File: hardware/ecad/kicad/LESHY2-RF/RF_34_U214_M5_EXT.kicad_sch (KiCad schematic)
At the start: 0 parts

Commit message: complete exact H2.3.1 RF power hierarchy
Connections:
- no-connect marks 0 -> 26

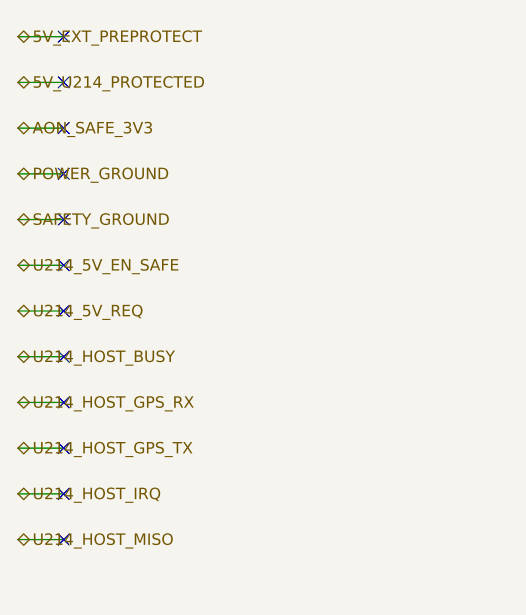
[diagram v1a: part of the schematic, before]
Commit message: complete exact H2.3.4 power rails
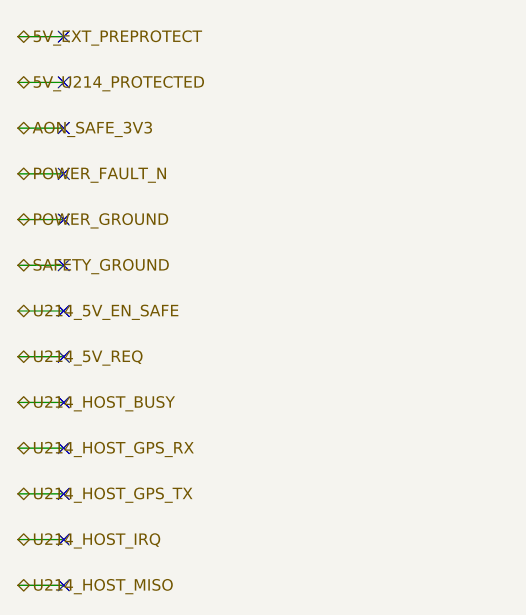
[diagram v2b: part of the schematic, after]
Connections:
- no-connect marks 26 -> 27
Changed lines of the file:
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@@
 	(no_connect (at 25.40 35.56)
 	)
-	(hierarchical_label "POWER_GROUND"
+	(hierarchical_label "POWER_FAULT_N"
 		(shape bidirectional)
 		(at 20.32 40.64 0)
@@
 	(no_connect (at 25.40 40.64)
 	)
-	(hierarchical_label "SAFETY_GROUND"
+	(hierarchical_label "POWER_GROUND"
 		(shape bidirectional)
 		(at 20.32 45.72 0)
@@
 	(no_connect (at 25.40 45.72)
 	)
-	(hierarchical_label "U214_5V_EN_SAFE"
+	(hierarchical_label "SAFETY_GROUND"
 		(shape bidirectional)
 		(at 20.32 50.80 0)
@@
 	(no_connect (at 25.40 50.80)
 	)
-	(hierarchical_label "U214_5V_REQ"
+	(hierarchical_label "U214_5V_EN_SAFE"
 		(shape bidirectional)
 		(at 20.32 55.88 0)
@@
 	(no_connect (at 25.40 55.88)
 	)
-	(hierarchical_label "U214_HOST_BUSY"
+	(hierarchical_label "U214_5V_REQ"
 		(shape bidirectional)
 		(at 20.32 60.96 0)
@@
 	(no_connect (at 25.40 60.96)
 	)
-	(hierarchical_label "U214_HOST_GPS_RX"
+	(hierarchical_label "U214_HOST_BUSY"
 		(shape bidirectional)
 		(at 20.32 66.04 0)
@@
 	(no_connect (at 25.40 66.04)
 	)
-	(hierarchical_label "U214_HOST_GPS_TX"
+	(hierarchical_label "U214_HOST_GPS_RX"
 		(shape bidirectional)
 		(at 20.32 71.12 0)
@@
 	(no_connect (at 25.40 71.12)
 	)
-	(hierarchical_label "U214_HOST_IRQ"
+	(hierarchical_label "U214_HOST_GPS_TX"
 		(shape bidirectional)
 		(at 20.32 76.20 0)
@@
 	(no_connect (at 25.40 76.20)
 	)
-	(hierarchical_label "U214_HOST_MISO"
+	(hierarchical_label "U214_HOST_IRQ"
 		(shape bidirectional)
 		(at 20.32 81.28 0)
@@
 	(no_connect (at 25.40 81.28)
 	)
+	(hierarchical_label "U214_HOST_MISO"
+		(shape bidirectional)
+		(at 20.32 86.36 0)
+		(effects (font (size 1.27 1.27)))
+	)
+	(wire
+		(pts (xy 20.32 86.36) (xy 25.40 86.36))
+		(stroke (width 0) (type default))
+	)
+	(no_connect (at 25.40 86.36)
+	)
 	(hierarchical_label "U214_HOST_MOSI"

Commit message: complete exact H2.3.8 U214 and M5 expansion sheet
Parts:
- added C1: TDK C1005X7R1H104K050BB, Capacitor_SMD:C_0402_1005Metric, symbol Leshy2:RF34_U214_I2C_ISO_BYPASS
- added C10: Murata GRM21BR71E225KE11L, Capacitor_SMD:C_0805_2012Metric, symbol Leshy2:RF34_UNIT_OUTPUT_CAP
- added C11: TDK C1005X7R1H104K050BB, Capacitor_SMD:C_0402_1005Metric, symbol Leshy2:RF34_UNIT_SUPERVISOR_BYPASS
- added C12: Murata GRM155R71H103KA88D, Capacitor_SMD:C_0402_1005Metric, symbol Leshy2:RF34_UNIT_SUPERVISOR_CT
- added C13: TDK C1005X7R1H104K050BB, Capacitor_SMD:C_0402_1005Metric, symbol Leshy2:RF34_UNIT_SIGNAL_ISO_VCCA_BYPASS
- added C14: TDK C1005X7R1H104K050BB, Capacitor_SMD:C_0402_1005Metric, symbol Leshy2:RF34_UNIT_SIGNAL_ISO_VCCB_BYPASS
- added C2: TDK C1005X7R1H104K050BB, Capacitor_SMD:C_0402_1005Metric, symbol Leshy2:RF34_U214_HOST_BUFFER_A_BYPASS
- added C3: TDK C1005X7R1H104K050BB, Capacitor_SMD:C_0402_1005Metric, symbol Leshy2:RF34_U214_HOST_BUFFER_B_BYPASS
- added C4: TDK C1005X7R1H104K050BB, Capacitor_SMD:C_0402_1005Metric, symbol Leshy2:RF34_U214_RETURN_BUFFER_BYPASS
- added C5: TDK C1005X7R1H104K050BB, Capacitor_SMD:C_0402_1005Metric, symbol Leshy2:RF34_U214_SUPERVISOR_BYPASS
- added C6: Murata GRM155R71H103KA88D, Capacitor_SMD:C_0402_1005Metric, symbol Leshy2:RF34_U214_SUPERVISOR_CT
- added C7: Murata GRM155R71H472KA01D, Capacitor_SMD:C_0402_1005Metric, symbol Leshy2:RF34_UNIT_DVDT_CAP
- added C8: Murata GRM188R71E224KA88D, Capacitor_SMD:C_0603_1608Metric, symbol Leshy2:RF34_UNIT_ITIMER_CAP
- added C9: Murata GRM21BR71E225KE11L, Capacitor_SMD:C_0805_2012Metric, symbol Leshy2:RF34_UNIT_INPUT_CAP
- added J1: Samtec HLE-107-02-G-DV-PE-LC, Connector_Samtec_HLE_THT:Samtec_HLE-107-02-xx-DV-PE-LC_2x07_P2.54mm_Horizontal, symbol Leshy2:RF34_U214_CONNECTOR
- added J2: 1125R-SMT-4P, Leshy2:1125R-SMT-4P, symbol Leshy2:RF34_UNIT_CONNECTOR
- added R1: Yageo RC0402FR-072K2L, Resistor_SMD:R_0402_1005Metric, symbol Leshy2:RF34_U214_I2C_HOST_SDA_PULLUP
- added R10: Panasonic ERJ-2RKF22R0X, Resistor_SMD:R_0402_1005Metric, symbol Leshy2:RF34_U214_SERIES_GPS_TX
- added R11: Panasonic ERJ-2RKF22R0X, Resistor_SMD:R_0402_1005Metric, symbol Leshy2:RF34_U214_SERIES_MISO
- added R12: Yageo RC0402FR-0710KL, Resistor_SMD:R_0402_1005Metric, symbol Leshy2:RF34_U214_REQ_PULLDOWN
- added R13: Yageo RC0402FR-0710KL, Resistor_SMD:R_0402_1005Metric, symbol Leshy2:RF34_UNIT_REQ_PULLDOWN
- added R14: Yageo RC0402FR-07110KL, Resistor_SMD:R_0402_1005Metric, symbol Leshy2:RF34_U214_SUPERVISOR_SENSE_TOP
- added R15: Yageo RC0402FR-07220KL, Resistor_SMD:R_0402_1005Metric, symbol Leshy2:RF34_U214_SUPERVISOR_SENSE_BOTTOM
- added R16: Yageo RC0402FR-0710KL, Resistor_SMD:R_0402_1005Metric, symbol Leshy2:RF34_U214_SUPERVISOR_PULLUP
- added R17: Yageo RC0402FR-072K21L, Resistor_SMD:R_0402_1005Metric, symbol Leshy2:RF34_UNIT_RILM
- added R18: Yageo RC0402FR-07169KL, Resistor_SMD:R_0402_1005Metric, symbol Leshy2:RF34_UNIT_OVLO_TOP
- added R19: Yageo RC0402FR-0747KL, Resistor_SMD:R_0402_1005Metric, symbol Leshy2:RF34_UNIT_OVLO_BOTTOM
- added R2: Yageo RC0402FR-072K2L, Resistor_SMD:R_0402_1005Metric, symbol Leshy2:RF34_U214_I2C_HOST_SCL_PULLUP
- added R20: Yageo RC0603FR-071KL, Resistor_SMD:R_0603_1608Metric, symbol Leshy2:RF34_UNIT_BLEEDER
- added R21: Yageo RC0402FR-07110KL, Resistor_SMD:R_0402_1005Metric, symbol Leshy2:RF34_UNIT_SUPERVISOR_SENSE_TOP
- added R22: Yageo RC0402FR-07220KL, Resistor_SMD:R_0402_1005Metric, symbol Leshy2:RF34_UNIT_SUPERVISOR_SENSE_BOTTOM
- added R23: Yageo RC0402FR-0710KL, Resistor_SMD:R_0402_1005Metric, symbol Leshy2:RF34_UNIT_SUPERVISOR_PULLUP
- added R24: Yageo RC0402FR-0710KL, Resistor_SMD:R_0402_1005Metric, symbol Leshy2:RF34_UNIT_SIGNAL_ISO_OE_PULLDOWN
- added R3: Panasonic ERJ-2RKF22R0X, Resistor_SMD:R_0402_1005Metric, symbol Leshy2:RF34_U214_SERIES_RST
- added R4: Panasonic ERJ-2RKF22R0X, Resistor_SMD:R_0402_1005Metric, symbol Leshy2:RF34_U214_SERIES_GPS_RX
- added R5: Panasonic ERJ-2RKF22R0X, Resistor_SMD:R_0402_1005Metric, symbol Leshy2:RF34_U214_SERIES_SCK
- added R6: Panasonic ERJ-2RKF22R0X, Resistor_SMD:R_0402_1005Metric, symbol Leshy2:RF34_U214_SERIES_MOSI
- added R7: Panasonic ERJ-2RKF22R0X, Resistor_SMD:R_0402_1005Metric, symbol Leshy2:RF34_U214_SERIES_NSS
- added R8: Panasonic ERJ-2RKF22R0X, Resistor_SMD:R_0402_1005Metric, symbol Leshy2:RF34_U214_SERIES_BUSY
- added R9: Panasonic ERJ-2RKF22R0X, Resistor_SMD:R_0402_1005Metric, symbol Leshy2:RF34_U214_SERIES_IRQ
- added U1: TCA4307DGKR, Package_SO:VSSOP-8_3x3mm_P0.65mm, symbol Leshy2:RF34_U214_I2C_ISO
- added U10: TPS3808G33DBVR, Package_TO_SOT_SMD:SOT-23-6, symbol Leshy2:RF34_UNIT_SUPERVISOR
- added U11: Texas Instruments TXS0102DCUR, Package_SO:VSSOP-8_2.3x2mm_P0.5mm, symbol Leshy2:RF34_UNIT_SIGNAL_ISO
- added U12: Texas Instruments TPD4E05U06DQAR, Package_SON:USON-10_2.5x1.0mm_P0.5mm, symbol Leshy2:RF34_UNIT_ESD
- added U2: Nexperia 74LVC126APW,118, Package_SO:TSSOP-14_4.4x5mm_P0.65mm, symbol Leshy2:RF34_U214_HOST_BUFFER_A
- added U3: Nexperia 74LVC126APW,118, Package_SO:TSSOP-14_4.4x5mm_P0.65mm, symbol Leshy2:RF34_U214_HOST_BUFFER_B
- added U4: Nexperia 74LVC126APW,118, Package_SO:TSSOP-14_4.4x5mm_P0.65mm, symbol Leshy2:RF34_U214_RETURN_BUFFER
- added U5: Texas Instruments TPD4E05U06DQAR, Package_SON:USON-10_2.5x1.0mm_P0.5mm, symbol Leshy2:RF34_U214_ESD_A
- added U6: Texas Instruments TPD4E05U06DQAR, Package_SON:USON-10_2.5x1.0mm_P0.5mm, symbol Leshy2:RF34_U214_ESD_B
- added U7: Texas Instruments TPD4E05U06DQAR, Package_SON:USON-10_2.5x1.0mm_P0.5mm, symbol Leshy2:RF34_U214_ESD_C
- added U8: TPS3808G33DBVR, Package_TO_SOT_SMD:SOT-23-6, symbol Leshy2:RF34_U214_SUPERVISOR
- added U9: Texas Instruments TPS259470LRPWR, Leshy2:TI-RPW0010A-VQFN-HR-10, symbol Leshy2:RF34_UNIT_EFUSE
- added X1: M5Stack U214 Cap LoRa-1262, symbol Leshy2:RF34_U214
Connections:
- net 3V3_MAIN: now also C1.1 (END_1), C13.1 (END_1), C14.1 (END_1), C2.1 (END_1), C3.1 (END_1), C4.1 (END_1), R1.1 (END_1), R16.1 (END_1), R2.1 (END_1), R23.1 (END_1), U1.8 (VCC), U11.1 (VCCA), U11.7 (VCCB), U2.14 (VCC), U3.14 (VCC), U4.14 (VCC)
- net 5V_EXT_PREPROTECT: now also C9.1 (END_1), R18.1 (END_1), U9.5 (IN)
- net 5V_U214_PROTECTED: now also J1.7 (PIN_7), R14.1 (END_1), X1.7 (5V_IN)
- net AON_SAFE_3V3: now also C11.1 (END_1), C5.1 (END_1), U10.6 (VDD), U8.6 (VDD)
- net POWER_FAULT_N: now also U9.4 (FLT)
- net POWER_GROUND: now also C1.2 (END_2), C10.2 (END_2), C13.2 (END_2), C14.2 (END_2), C2.2 (END_2), C3.2 (END_2), C4.2 (END_2), C7.2 (END_2), C8.2 (END_2), C9.2 (END_2), J1.6 (PIN_6), J2.1 (GND), R12.2 (END_2), R13.2 (END_2), R17.2 (END_2), R19.2 (END_2), R20.2 (END_2), R24.2 (END_2), U1.4 (GND), U11.4 (GND), U12.3 (GND_3), U12.8 (GND_8), U2.7 (GND), U3.10 (3OE), U3.12 (4A), U3.13 (4OE), U3.4 (2OE), U3.5 (2A), U3.7 (GND), U3.9 (3A), U4.7 (GND), U5.3 (GND_3), U5.8 (GND_8), U6.3 (GND_3), U6.8 (GND_8), U7.3 (GND_3), U7.8 (GND_8), U9.8 (GND), X1.6 (GND)
- net SAFETY_GROUND: now also C11.2 (END_2), C12.2 (END_2), C5.2 (END_2), C6.2 (END_2), R15.2 (END_2), R22.2 (END_2), U10.2 (GND), U8.2 (GND)
- net U214_5V_EN_SAFE: now also U8.3 (MR_N)
- net U214_5V_REQ: now also R12.1 (END_1)
- net U214_HOST_BUSY: now also R8.2 (END_2)
- net U214_HOST_GPS_RX: now also R10.2 (END_2)
- net U214_HOST_GPS_TX: now also U2.5 (2A)
- net U214_HOST_IRQ: now also R9.2 (END_2)
- net U214_HOST_MISO: now also R11.2 (END_2)
- net U214_HOST_MOSI: now also U2.12 (4A)
- net U214_HOST_NSS_N: now also U3.2 (1A)
- net U214_HOST_RST_N: now also U2.2 (1A)
- net U214_HOST_SCK: now also U2.9 (3A)
- net U214_I2C_READY: now also U1.5 (READY)
- net U214_I2C_SCL_IN: now also R2.2 (END_2), U1.3 (SCLIN)
- net U214_I2C_SDA_IN: now also R1.2 (END_2), U1.6 (SDAIN)
- net U214_PIN5_PROFILE: now also J1.5 (PIN_5), U7.5 (D2_MINUS), X1.5 (5V_OUT)
- net UNIT_5V_EN_SAFE: now also U10.3 (MR_N), U9.1 (EN_UVLO)
- net UNIT_5V_REQ: now also R13.1 (END_1)
- net UNIT_HOST_SIG0: now also U11.2 (A1)
- net UNIT_HOST_SIG1: now also U11.3 (A2)
- net UNIT_READY: now also R23.2 (END_2), R24.1 (END_1), U10.1 (RESET_N), U11.8 (OE)
- new net 5V_UNIT_PROTECTED: C10.1 (END_1), J2.2 (5V), R20.1 (END_1), R21.1 (END_1), U9.6 (OUT)
- new net U214_5V_SENSE: R14.2 (END_2), R15.1 (END_1), U8.5 (SENSE)
- new net U214_BUSY_BUFFERED: R8.1 (END_1), U4.3 (1Y)
- new net U214_BUSY_CONNECTOR: J1.10 (PIN_10), U4.2 (1A), U6.5 (D2_MINUS), X1.10 (LORA_BUSY)
- new net U214_GPS_RX_BUFFERED: R4.1 (END_1), U2.6 (2Y)
- new net U214_GPS_RX_CONNECTOR: J1.2 (PIN_2), R4.2 (END_2), U5.5 (D2_MINUS), X1.2 (GPS_RX)
- new net U214_GPS_TX_BUFFERED: R10.1 (END_1), U4.8 (3Y)
- new net U214_GPS_TX_CONNECTOR: J1.1 (PIN_1), U4.9 (3A), U7.2 (D1_MINUS), X1.1 (GPS_TX)
- new net U214_I2C_SCL_OUT: J1.3 (PIN_3), U1.2 (SCLOUT), U5.2 (D1_MINUS), X1.3 (SCL)
- new net U214_I2C_SDA_OUT: J1.4 (PIN_4), U1.7 (SDAOUT), U5.1 (D1_PLUS), X1.4 (SDA)
- new net U214_IRQ_BUFFERED: R9.1 (END_1), U4.6 (2Y)
- new net U214_IRQ_CONNECTOR: J1.9 (PIN_9), U4.5 (2A), U7.1 (D1_PLUS), X1.9 (LORA_IRQ)
- new net U214_MISO_BUFFERED: R11.1 (END_1), U4.11 (4Y)
- new net U214_MISO_CONNECTOR: J1.13 (PIN_13), U4.12 (4A), U7.4 (D2_PLUS), X1.13 (MISO)
- new net U214_MOSI_BUFFERED: R6.1 (END_1), U2.11 (4Y)
- new net U214_MOSI_CONNECTOR: J1.12 (PIN_12), R6.2 (END_2), U6.2 (D1_MINUS), X1.12 (MOSI)
- new net U214_NSS_BUFFERED: R7.1 (END_1), U3.3 (1Y)
- new net U214_NSS_CONNECTOR: J1.14 (PIN_14), R7.2 (END_2), U6.4 (D2_PLUS), X1.14 (NSS)
- new net U214_READY: R16.2 (END_2), U1.1 (EN), U2.1 (1OE), U2.10 (3OE), U2.13 (4OE), U2.4 (2OE), U3.1 (1OE), U4.1 (1OE), U4.10 (3OE), U4.13 (4OE), U4.4 (2OE), U8.1 (RESET_N)
- new net U214_READY_DELAY: C6.1 (END_1), U8.4 (CT)
- new net U214_RST_BUFFERED: R3.1 (END_1), U2.3 (1Y)
- new net U214_RST_CONNECTOR: J1.8 (PIN_8), R3.2 (END_2), U5.4 (D2_PLUS), X1.8 (LORA_RST)
- new net U214_SCK_BUFFERED: R5.1 (END_1), U2.8 (3Y)
- new net U214_SCK_CONNECTOR: J1.11 (PIN_11), R5.2 (END_2), U6.1 (D1_PLUS), X1.11 (SCK)
- new net UNIT_5V_CURRENT_MONITOR: R17.1 (END_1), U9.9 (ILM)
- new net UNIT_5V_SENSE: R21.2 (END_2), R22.1 (END_1), U10.5 (SENSE)
- new net UNIT_CONNECTOR_SIG0: J2.3 (SIG0), U11.6 (B1), U12.1 (D1_PLUS)
- new net UNIT_CONNECTOR_SIG1: J2.4 (SIG1), U11.5 (B2), U12.2 (D1_MINUS)
- new net UNIT_EFUSE_DVDT: C7.1 (END_1), U9.7 (DVDT)
- new net UNIT_EFUSE_ITIMER: C8.1 (END_1), U9.10 (ITIMER)
- new net UNIT_EFUSE_OVLO_SENSE: R18.2 (END_2), R19.1 (END_1), U9.2 (OVLO)
- new net UNIT_READY_DELAY: C12.1 (END_1), U10.4 (CT)
- no-connect marks 27 -> 22
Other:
- title: (none) -> Leshy2 — isolated U214 Cap-Bus and native M5 Unit expansion

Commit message: complete H2 schematic review package
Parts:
- renumbered C1 to C34001, C2 to C34002, C3 to C34003, C4 to C34004, C5 to C34005, C6 to C34006, C7 to C34007, C8 to C34008, C9 to C34009, C10 to C34010, C11 to C34011, C12 to C34012, C13 to C34013, C14 to C34014, J1 to J34001, J2 to J34002, R1 to R34001, R2 to R34002, R3 to R34003, R4 to R34004, R5 to R34005, R6 to R34006, R7 to R34007, R8 to R34008, R9 to R34009, R10 to R34010, R11 to R34011, R12 to R34012, R13 to R34013, R14 to R34014, R15 to R34015, R16 to R34016, R17 to R34017, R18 to R34018, R19 to R34019, R20 to R34020, R21 to R34021, R22 to R34022, R23 to R34023, R24 to R34024, U1 to U34001, U2 to U34002, U3 to U34003, U4 to U34004, U5 to U34005, U6 to U34006, U7 to U34007, U8 to U34008, U9 to U34009, U10 to U34010, U11 to U34011, U12 to U34012, X1 to X34001

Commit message: docs: complete H3.1 steady power verification
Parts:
- R34017: value Yageo RC0402FR-072K21L -> Yageo RC0402FR-071K82L
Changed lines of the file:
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@@
 			(effects (font (size 1.27 1.27)))
 		)
-		(property "Value" "Yageo RC0402FR-072K21L"
+		(property "Value" "Yageo RC0402FR-071K82L"
 			(at 320.04 135.89 0)
 			(show_name no)
@@
 			(effects (font (size 1.27 1.27)))
 		)
-		(property "Description" "2_21kohm_1pct_0402_efuse_current_limit_resistor"
+		(property "Description" "1_82kohm_1pct_0402_efuse_current_limit_resistor"
 			(at 320.04 130.81 0)
 			(show_name no)

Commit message: Optimize H1 display and stocked BOM routes
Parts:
- C34001, C34002, C34003, C34004, C34005, C34011, C34013, C34014: value TDK C1005X7R1H104K050BB -> Yageo CC0402KRX7R9BB104
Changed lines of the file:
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@@
 			(effects (font (size 1.27 1.27)))
 		)
-		(property "Value" "TDK C1005X7R1H104K050BB"
+		(property "Value" "Yageo CC0402KRX7R9BB104"
 			(at 208.28 44.45 0)
 			(show_name no)
@@
 			(effects (font (size 1.27 1.27)))
 		)
-		(property "Value" "TDK C1005X7R1H104K050BB"
+		(property "Value" "Yageo CC0402KRX7R9BB104"
 			(at 264.16 67.31 0)
 			(show_name no)
@@
 			(effects (font (size 1.27 1.27)))
 		)
-		(property "Value" "TDK C1005X7R1H104K050BB"
+		(property "Value" "Yageo CC0402KRX7R9BB104"
 			(at 320.04 67.31 0)
 			(show_name no)
@@
 			(effects (font (size 1.27 1.27)))
 		)
-		(property "Value" "TDK C1005X7R1H104K050BB"
+		(property "Value" "Yageo CC0402KRX7R9BB104"
 			(at 152.40 72.39 0)
 			(show_name no)
@@
 			(effects (font (size 1.27 1.27)))
 		)
-		(property "Value" "TDK C1005X7R1H104K050BB"
+		(property "Value" "Yageo CC0402KRX7R9BB104"
 			(at 40.64 125.73 0)
 			(show_name no)
@@
 			(effects (font (size 1.27 1.27)))
 		)
-		(property "Value" "TDK C1005X7R1H104K050BB"
+		(property "Value" "Yageo CC0402KRX7R9BB104"
 			(at 152.40 166.37 0)
 			(show_name no)
@@
 			(effects (font (size 1.27 1.27)))
 		)
-		(property "Value" "TDK C1005X7R1H104K050BB"
+		(property "Value" "Yageo CC0402KRX7R9BB104"
 			(at 320.04 181.61 0)
 			(show_name no)
@@
 			(effects (font (size 1.27 1.27)))
 		)
-		(property "Value" "TDK C1005X7R1H104K050BB"
+		(property "Value" "Yageo CC0402KRX7R9BB104"
 			(at 152.40 189.23 0)
 			(show_name no)

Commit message: Replace six pre-order resistor identities
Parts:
- R34001, R34002: value Yageo RC0402FR-072K2L -> UNI-ROYAL 0402WGF2201TCE
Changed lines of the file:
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@@
 			(effects (font (size 1.27 1.27)))
 		)
-		(property "Value" "Yageo RC0402FR-072K2L"
+		(property "Value" "UNI-ROYAL 0402WGF2201TCE"
 			(at 264.16 44.45 0)
 			(show_name no)
@@
 			(effects (font (size 1.27 1.27)))
 		)
-		(property "Value" "Yageo RC0402FR-072K2L"
+		(property "Value" "UNI-ROYAL 0402WGF2201TCE"
 			(at 320.04 44.45 0)
 			(show_name no)
